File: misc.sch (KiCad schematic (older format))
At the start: 38 parts, among them CN8 POWER_INPUT, CN9 LED_CONNECTOR, SW1 POWER_SWITCH, U10 NE555P, U12 74LS02, U7 L7812, U9 74LS06

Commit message: Closer and closer...
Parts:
- L3: footprint Inductor_THT:L_Axial_L7.0mm_D3.3mm_P12.70mm_Horizontal_Fastron_MICC -> Inductor_THT:L_Radial_D6.0mm_P4.00mm; MouserPN (none) -> 875-28C0236-0EW-10
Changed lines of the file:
@@
 F 0 "L3" V 6630 6845 50  0000 C CNN
 F 1 "FERRITE" V 6539 6845 50  0000 C CNN
-F 2 "Inductor_THT:L_Axial_L7.0mm_D3.3mm_P12.70mm_Horizontal_Fastron_MICC" H 6440 6845 50  0001 C CNN
+F 2 "Inductor_THT:L_Radial_D6.0mm_P4.00mm" H 6440 6845 50  0001 C CNN
 F 3 "~" H 6440 6845 50  0001 C CNN
+F 4 "875-28C0236-0EW-10" H 6440 6845 50  0001 C CNN "MouserPN"
 	1    6440 6845
 	0    -1   -1   0

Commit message: Replace joystick buffers with '245s This was done for economy of scale, as we already have other '245s onboard
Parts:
- C107: footprint Capacitor_THT:CP_Radial_D10.0mm_P5.00mm -> LittleSixteen:Axial_Cap_Dual
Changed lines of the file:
@@
 F 0 "C107" H 7750 2406 50  0000 R CNN
 F 1 "1000u/25V" H 7750 2315 50  0000 R CNN
-F 2 "Capacitor_THT:CP_Radial_D10.0mm_P5.00mm" H 7865 2360 50  0001 C CNN
+F 2 "LittleSixteen:Axial_Cap_Dual" H 7865 2360 50  0001 C CNN
 F 3 "~" H 7865 2360 50  0001 C CNN
 	1    7865 2360

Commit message: Make most ICs HCT
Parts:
- U12: value 74LS02 -> 74HCT02
- U7: Notes (none) -> VERY IMPORTANT!!! For 8580 use L7809
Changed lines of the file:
@@
 AR Path="/5E4A465A/660AD22F" Ref="U?"  Part="4"
 F 0 "U12" H 9805 6375 50  0000 C CNN
-F 1 "74LS02" H 9805 6284 50  0000 C CNN
+F 1 "74HCT02" H 9805 6284 50  0000 C CNN
 F 2 "LittleSixteen:DIP-14_W7.62mm_Socket_LongPads" H 9805 6050 50  0001 C CNN
 F 3 "http://www.ti.com/lit/gpn/sn74ls02" H 9805 6050 50  0001 C CNN
@@
 F 2 "Package_TO_SOT_THT:TO-220-3_Vertical" H 5070 6695 50  0001 L CIN
 F 3 "http://www.st.com/content/ccc/resource/technical/document/datasheet/41/4f/b3/b0/12/d4/47/88/CD00000444.pdf/files/CD00000444.pdf/jcr:content/translations/en.CD00000444.pdf" H 5045 6795 50  0001 C CNN
+F 4 "VERY IMPORTANT!!! For 8580 use L7809" H 5045 6845 50  0001 C CNN "Notes"
 	1    5045 6845
 	1    0    0    -1

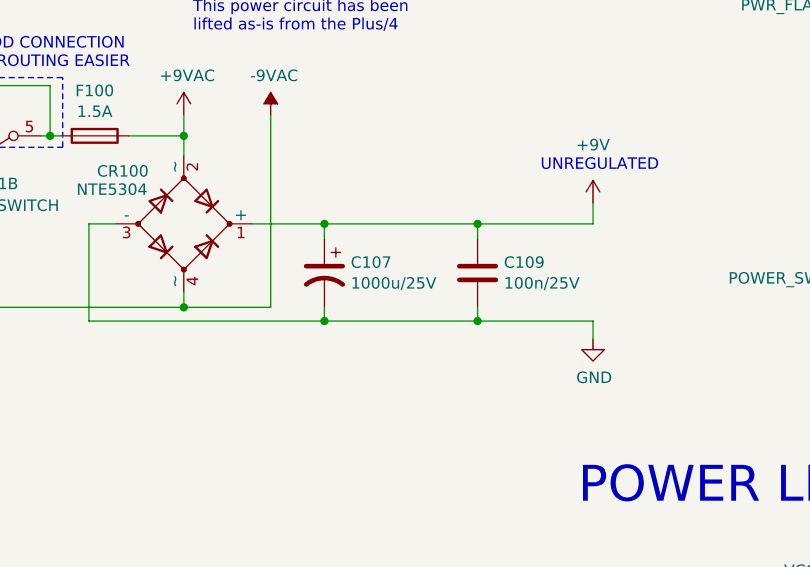
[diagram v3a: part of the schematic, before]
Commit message: Replace L1 with ferrite
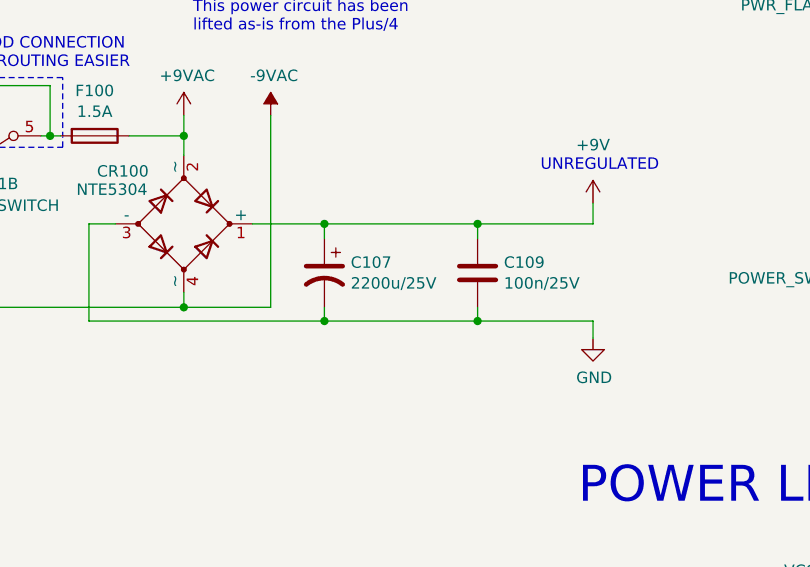
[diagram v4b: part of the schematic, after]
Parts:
- C107: value 1000u/25V -> 2200u/25V
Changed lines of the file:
@@
 AR Path="/5EACE220/62DDC32C" Ref="C107"  Part="1"
 F 0 "C107" H 7750 2406 50  0000 R CNN
-F 1 "1000u/25V" H 7750 2315 50  0000 R CNN
+F 1 "2200u/25V" H 7750 2315 50  0000 R CNN
 F 2 "LittleSixteen:Axial_Cap_Dual" H 7865 2360 50  0001 C CNN
 F 3 "~" H 7865 2360 50  0001 C CNN

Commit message: Use fatter footprint for D87/88
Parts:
- D87, D88: footprint LittleSixteen:D_DO-35_SOD27_P5.08mm_Vertical_KathodeUp -> LittleSixteen:D_DO-41_SOD81_P5.08mm_Vertical_KathodeUp
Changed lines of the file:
@@
 F 0 "D87" H 2970 6628 50  0000 C CNN
 F 1 "1n4001" H 2970 6719 50  0000 C CNN
-F 2 "LittleSixteen:D_DO-35_SOD27_P5.08mm_Vertical_KathodeUp" H 2970 6845 50  0001 C CNN
+F 2 "LittleSixteen:D_DO-41_SOD81_P5.08mm_Vertical_KathodeUp" H 2970 6845 50  0001 C CNN
 F 3 "~" H 2970 6845 50  0001 C CNN
 	1    2970 6845
@@
 F 0 "D88" H 3630 6628 50  0000 C CNN
 F 1 "1n4001" H 3630 6719 50  0000 C CNN
-F 2 "LittleSixteen:D_DO-35_SOD27_P5.08mm_Vertical_KathodeUp" H 3630 6845 50  0001 C CNN
+F 2 "LittleSixteen:D_DO-41_SOD81_P5.08mm_Vertical_KathodeUp" H 3630 6845 50  0001 C CNN
 F 3 "~" H 3630 6845 50  0001 C CNN
 	1    3630 6845

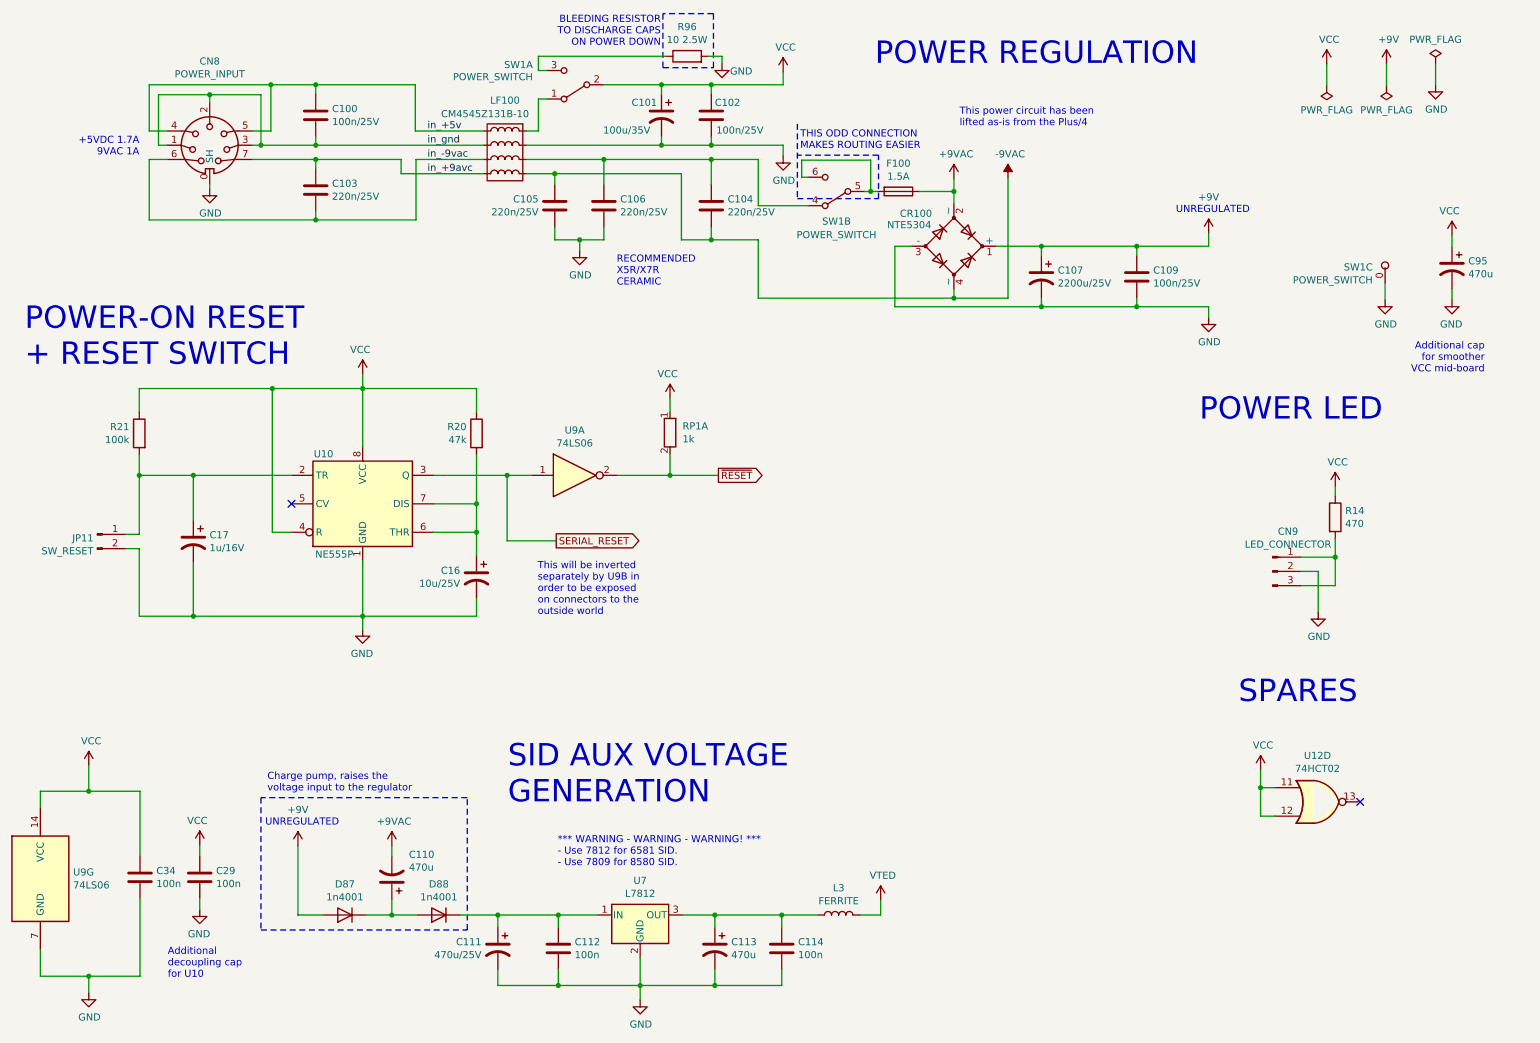
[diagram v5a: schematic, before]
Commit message: Add testpoints
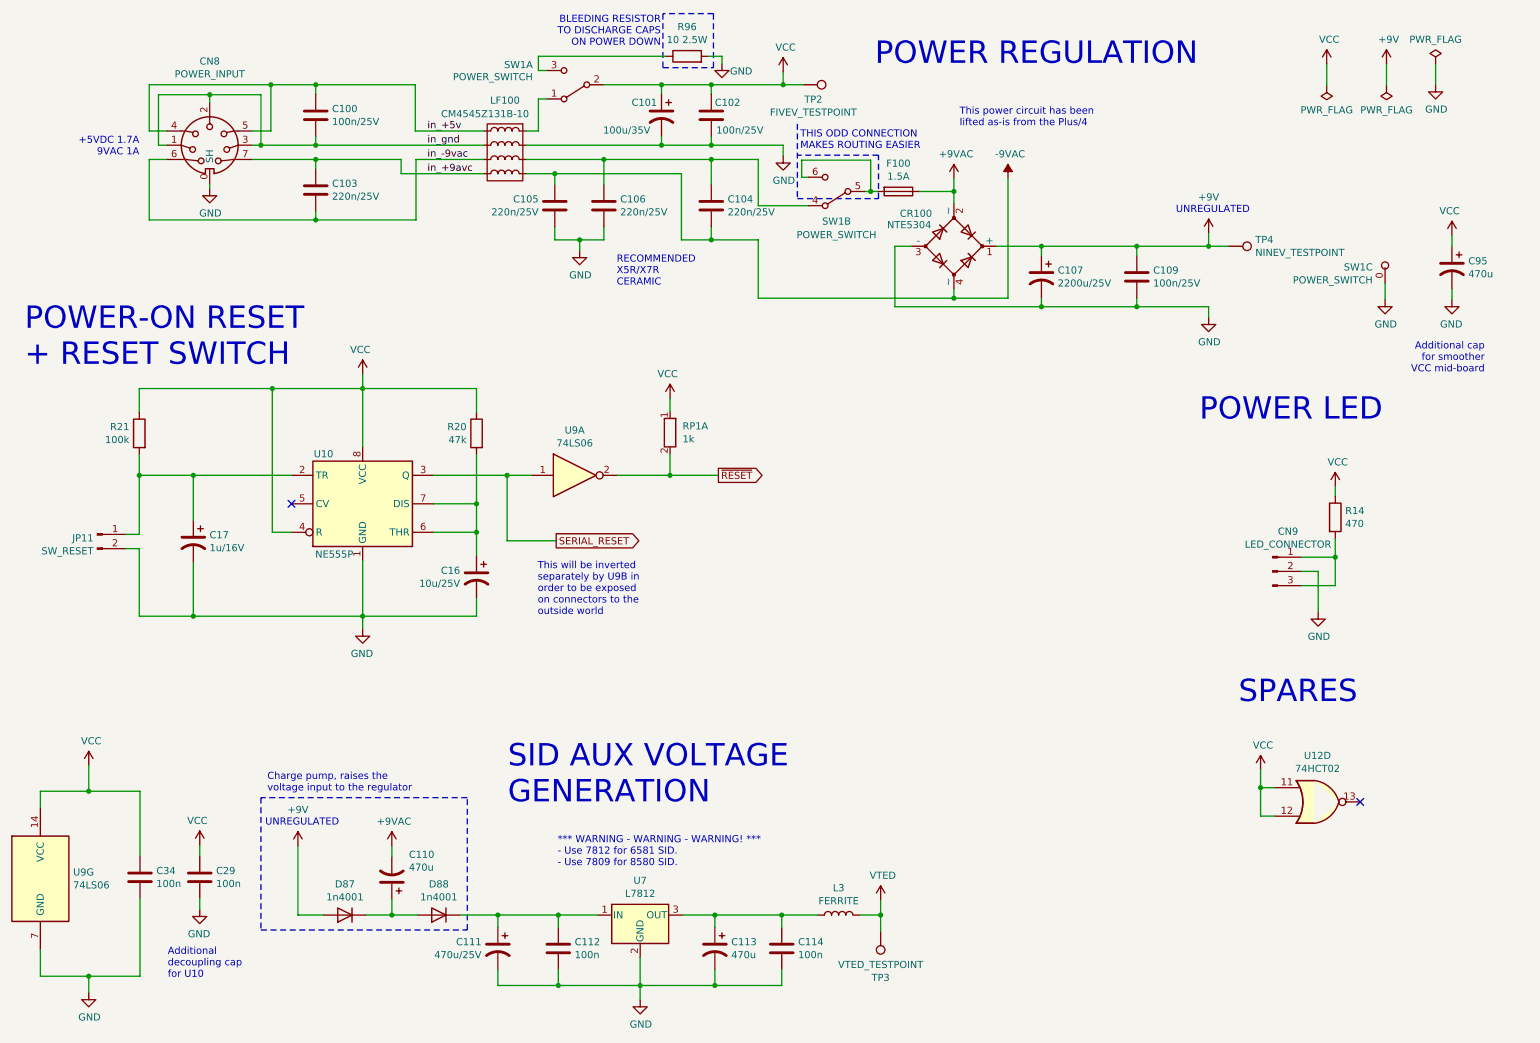
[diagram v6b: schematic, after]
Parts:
- added TP2: FIVEV_TESTPOINT, TestPoint:TestPoint_Pad_D2.0mm, symbol Connector:TestPoint
- added TP3: VTED_TESTPOINT, TestPoint:TestPoint_Pad_D2.0mm, symbol Connector:TestPoint
- added TP4: NINEV_TESTPOINT, TestPoint:TestPoint_Pad_D2.0mm, symbol Connector:TestPoint
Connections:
- net +9V: now also TP4.1
- net VCC: now also TP2.1
- net VTED: now also TP3.1
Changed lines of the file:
@@
 	1    0    0    -1
 $EndComp
+$Comp
+L Connector:TestPoint TP?
+U 1 1 64EE4596
+P 6735 6960
+AR Path="/5DE044CB/64EE4596" Ref="TP?"  Part="1"
+AR Path="/5EACE220/64EE4596" Ref="TP3"  Part="1"
+F 0 "TP3" H 6735 7285 50  0000 C CNN
+F 1 "VTED_TESTPOINT" H 6735 7194 50  0000 C CNN
+F 2 "TestPoint:TestPoint_Pad_D2.0mm" H 6935 6960 50  0001 C CNN
+F 3 "~" H 6935 6960 50  0001 C CNN
+	1    6735 6960
+	-1   0    0    1
+$EndComp
+Wire Wire Line
+	6735 6960 6735 6845
+Connection ~ 6735 6845
+$Comp
+L Connector:TestPoint TP?
+U 1 1 64EF6F17
+P 6190 1010
+AR Path="/5DE044CB/64EF6F17" Ref="TP?"  Part="1"
+AR Path="/5EACE220/64EF6F17" Ref="TP2"  Part="1"
+F 0 "TP2" V 6293 1082 50  0000 C CNN
+F 1 "FIVEV_TESTPOINT" V 6384 1082 50  0000 C CNN
+F 2 "TestPoint:TestPoint_Pad_D2.0mm" H 6390 1010 50  0001 C CNN
+F 3 "~" H 6390 1010 50  0001 C CNN
+	1    6190 1010
+	0    1    1    0
+$EndComp
+Wire Wire Line
+	6050 1010 6190 1010
+Connection ~ 6050 1010
+$Comp
+L Connector:TestPoint TP?
+U 1 1 64F0CBEF
+P 9180 2145
+AR Path="/5DE044CB/64F0CBEF" Ref="TP?"  Part="1"
+AR Path="/5EACE220/64F0CBEF" Ref="TP4"  Part="1"
+F 0 "TP4" V 9134 2333 50  0000 L CNN
+F 1 "NINEV_TESTPOINT" V 9225 2333 50  0000 L CNN
+F 2 "TestPoint:TestPoint_Pad_D2.0mm" H 9380 2145 50  0001 C CNN
+F 3 "~" H 9380 2145 50  0001 C CNN
+	1    9180 2145
+	0    1    1    0
+$EndComp
+Wire Wire Line
+	9040 2145 9180 2145
+Connection ~ 9040 2145
 $EndSCHEMATC

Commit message: Rationalize BOM There should be no significant changes on both schematics on PCB, just some values and something on the silkscreen
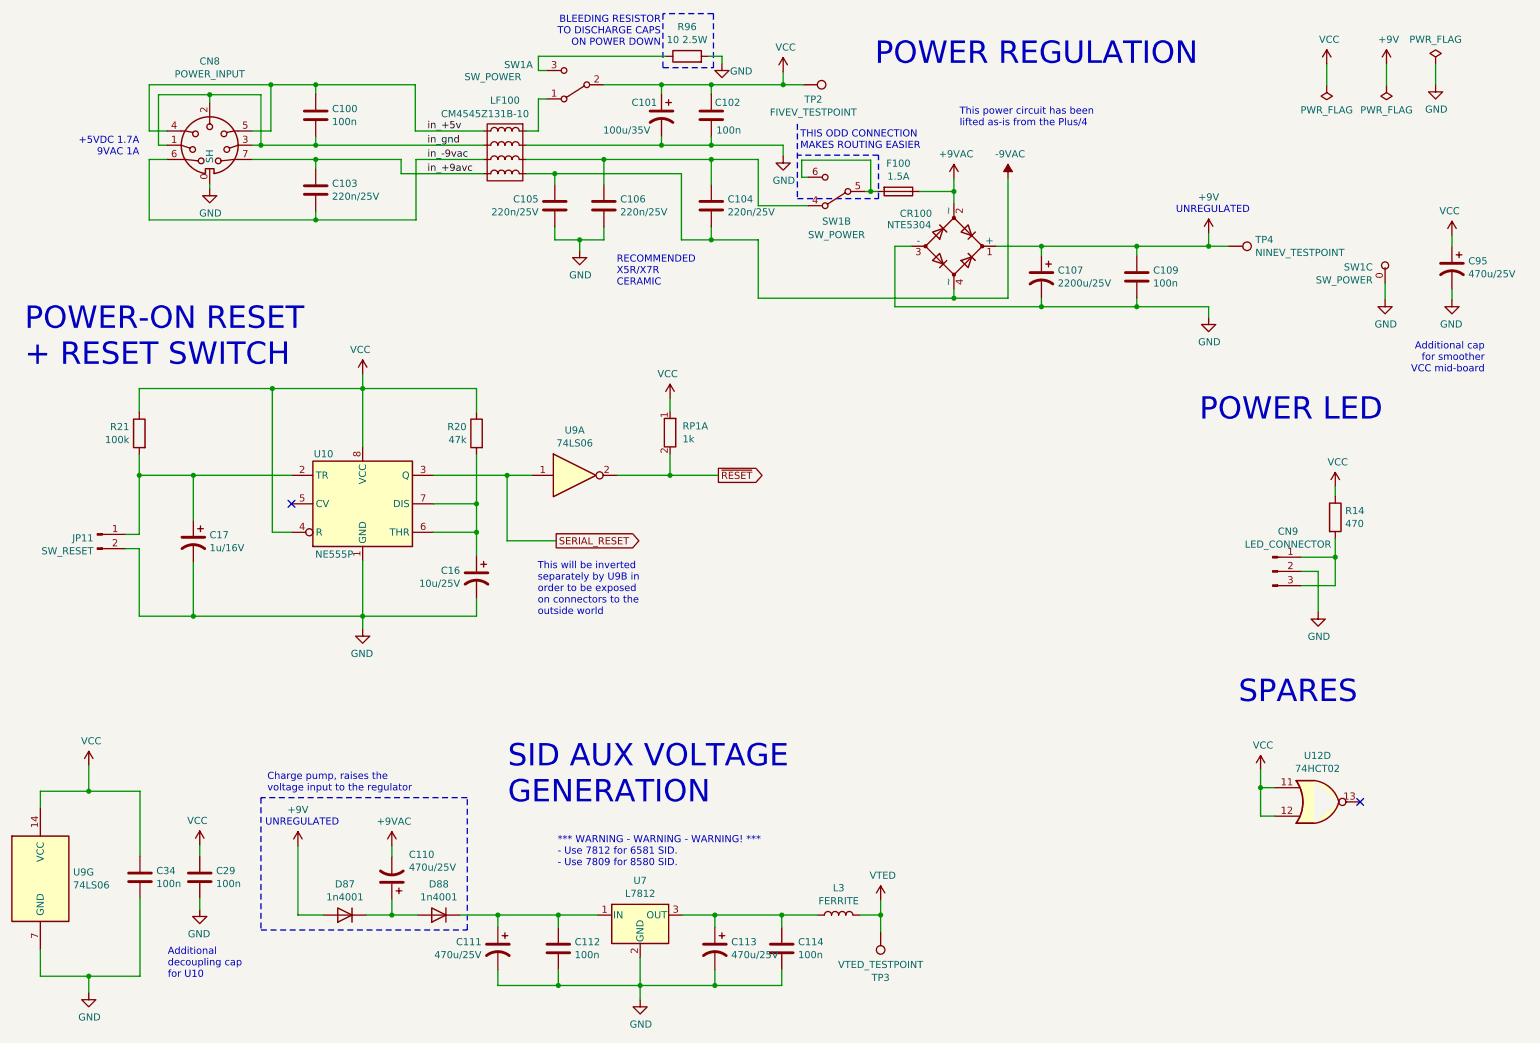
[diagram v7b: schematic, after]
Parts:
- C100, C102, C109: value 100n/25V -> 100n; MouserPN (none) -> 810-FG28X7R1H104KNT0
- C110, C113: value 470u -> 470u/25V; MouserPN 710-860020474013 -> 710-860010474013
- C111: MouserPN (none) -> 710-860010474013
- C112, C114, C29, C34: MouserPN (none) -> 810-FG28X7R1H104KNT0
- C95: value 470u -> 470u/25V; MouserPN (none) -> 710-860010575013
- RP1: Notes (none) -> Bussed
- SW1: value POWER_SWITCH -> SW_POWER
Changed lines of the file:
@@
 F 2 "Capacitor_THT:C_Disc_D8.0mm_W2.5mm_P5.00mm" H 1568 6430 50  0001 C CNN
 F 3 "~" H 1530 6580 50  0001 C CNN
+F 4 "810-FG28X7R1H104KNT0" H 1530 6580 50  0001 C CNN "MouserPN"
 	1    1530 6580
 	1    0    0    -1
@@
 F 2 "Capacitor_THT:C_Disc_D8.0mm_W2.5mm_P5.00mm" H 1988 6430 50  0001 C CNN
 F 3 "~" H 1950 6580 50  0001 C CNN
+F 4 "810-FG28X7R1H104KNT0" H 1950 6580 50  0001 C CNN "MouserPN"
 	1    1950 6580
 	-1   0    0    -1
@@
 P 10280 2330
 F 0 "SW1" H 10367 2368 50  0000 L CNN
-F 1 "POWER_SWITCH" H 10367 2277 50  0000 L CNN
+F 1 "SW_POWER" H 10367 2277 50  0000 L CNN
 F 2 "LittleSixteen:C64_PowerSwitch" H 10280 2330 50  0001 C CNN
 F 3 "~" H 10280 2330 50  0001 C CNN
@@
 P 2765 1225
 F 0 "C100" H 2880 1271 50  0000 L CNN
-F 1 "100n/25V" H 2880 1180 50  0000 L CNN
+F 1 "100n" H 2880 1180 50  0000 L CNN
 F 2 "Capacitor_THT:C_Disc_D8.0mm_W2.5mm_P5.00mm" H 2803 1075 50  0001 C CNN
 F 3 "~" H 2765 1225 50  0001 C CNN
+F 4 "810-FG28X7R1H104KNT0" H 2765 1225 50  0001 C CNN "MouserPN"
 	1    2765 1225
 	1    0    0    -1
@@
 P 5545 1225
 F 0 "C102" H 5570 1315 50  0000 L CNN
-F 1 "100n/25V" H 5580 1120 50  0000 L CNN
+F 1 "100n" H 5580 1120 50  0000 L CNN
 F 2 "Capacitor_THT:C_Disc_D8.0mm_W2.5mm_P5.00mm" H 5583 1075 50  0001 C CNN
 F 3 "~" H 5545 1225 50  0001 C CNN
+F 4 "810-FG28X7R1H104KNT0" H 5545 1225 50  0001 C CNN "MouserPN"
 	1    5545 1225
 	1    0    0    -1
@@
 P 8535 2360
 F 0 "C109" H 8650 2406 50  0000 L CNN
-F 1 "100n/25V" H 8650 2315 50  0000 L CNN
+F 1 "100n" H 8650 2315 50  0000 L CNN
 F 2 "Capacitor_THT:C_Disc_D8.0mm_W2.5mm_P5.00mm" H 8573 2210 50  0001 C CNN
 F 3 "~" H 8535 2360 50  0001 C CNN
+F 4 "810-FG28X7R1H104KNT0" H 8535 2360 50  0001 C CNN "MouserPN"
 	1    8535 2360
 	1    0    0    -1
@@
 AR Path="/5EACE220/634C97F7" Ref="C95"  Part="1"
 F 0 "C95" H 10635 2341 50  0000 R CNN
-F 1 "470u" H 10635 2250 50  0000 R CNN
+F 1 "470u/25V" H 10635 2250 50  0000 R CNN
 F 2 "Capacitor_THT:CP_Radial_D10.0mm_P5.00mm" H 10750 2295 50  0001 C CNN
 F 3 "~" H 10750 2295 50  0001 C CNN
+F 4 "710-860010575013" H 10750 2295 50  0001 C CNN "MouserPN"
 	1    10750 2295
 	-1   0    0    -1
@@
 P 4590 1010
 F 0 "SW1" H 4990 870 50  0000 C CNN
-F 1 "POWER_SWITCH" H 5170 955 50  0000 C CNN
+F 1 "SW_POWER" H 5170 955 50  0000 C CNN
 F 2 "LittleSixteen:C64_PowerSwitch" H 4590 1010 50  0001 C CNN
 F 3 "~" H 4590 1010 50  0001 C CNN
@@
 P 6425 1760
 F 0 "SW1" H 6425 1970 50  0000 C CNN
-F 1 "POWER_SWITCH" H 6425 2065 50  0000 C CNN
+F 1 "SW_POWER" H 6425 2065 50  0000 C CNN
 F 2 "LittleSixteen:C64_PowerSwitch" H 6425 1760 50  0001 C CNN
 F 3 "~" H 6425 1760 50  0001 C CNN
@@
 F 2 "Resistor_THT:R_Array_SIP6" V 5175 3455 50  0001 C CNN
 F 3 "http://www.vishay.com/docs/31509/csc.pdf" H 5255 3455 50  0001 C CNN
+F 4 "Bussed" H 5255 3455 50  0001 C CNN "Notes"
 	1    5255 3455
 	1    0    0    -1
@@
 F 2 "Capacitor_THT:C_Disc_D8.0mm_W2.5mm_P5.00mm" H 4508 6930 50  0001 C CNN
 F 3 "~" H 4470 7080 50  0001 C CNN
+F 4 "810-FG28X7R1H104KNT0" H 4470 7080 50  0001 C CNN "MouserPN"
 	1    4470 7080
 	1    0    0    -1
@@
 F 2 "Capacitor_THT:C_Disc_D8.0mm_W2.5mm_P5.00mm" H 6078 6930 50  0001 C CNN
 F 3 "~" H 6040 7080 50  0001 C CNN
+F 4 "810-FG28X7R1H104KNT0" H 6040 7080 50  0001 C CNN "MouserPN"
 	1    6040 7080
 	1    0    0    -1
@@
 F 2 "Capacitor_THT:CP_Radial_D8.0mm_P3.50mm" H 4045 7080 50  0001 C CNN
 F 3 "~" H 4045 7080 50  0001 C CNN
+F 4 "710-860010474013" H 4045 7080 50  0001 C CNN "MouserPN"
 	1    4045 7080
 	-1   0    0    -1
@@
 AR Path="/5EACE220/6530A0A3" Ref="C113"  Part="1"
 F 0 "C113" H 5455 7126 50  0000 R CNN
-F 1 "470u" H 5455 7035 50  0000 R CNN
+F 1 "470u/25V" H 5455 7035 50  0000 R CNN
 F 2 "Capacitor_THT:CP_Radial_D8.0mm_P3.50mm" H 5570 7080 50  0001 C CNN
 F 3 "~" H 5570 7080 50  0001 C CNN
-F 4 "710-860020474013" H 5570 7080 50  0001 C CNN "MouserPN"
+F 4 "710-860010474013" H 5570 7080 50  0001 C CNN "MouserPN"
 	1    5570 7080
 	-1   0    0    -1
@@
 AR Path="/5EACE220/652C0739" Ref="C110"  Part="1"
 F 0 "C110" H 3180 6420 50  0000 R CNN
-F 1 "470u" H 3180 6510 50  0000 R CNN
+F 1 "470u/25V" H 3180 6510 50  0000 R CNN
 F 2 "Capacitor_THT:CP_Radial_D8.0mm_P3.50mm" H 3300 6585 50  0001 C CNN
 F 3 "~" H 3300 6585 50  0001 C CNN
-F 4 "710-860020474013" H 3300 6585 50  0001 C CNN "MouserPN"
+F 4 "710-860010474013" H 3300 6585 50  0001 C CNN "MouserPN"
 	1    3300 6585
 	-1   0    0    1
